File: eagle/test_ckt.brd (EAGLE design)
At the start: 152.4 x 152.4 mm, 38 parts, among them IC1 LT1352PA, T1 2N3904, T2 2N3904

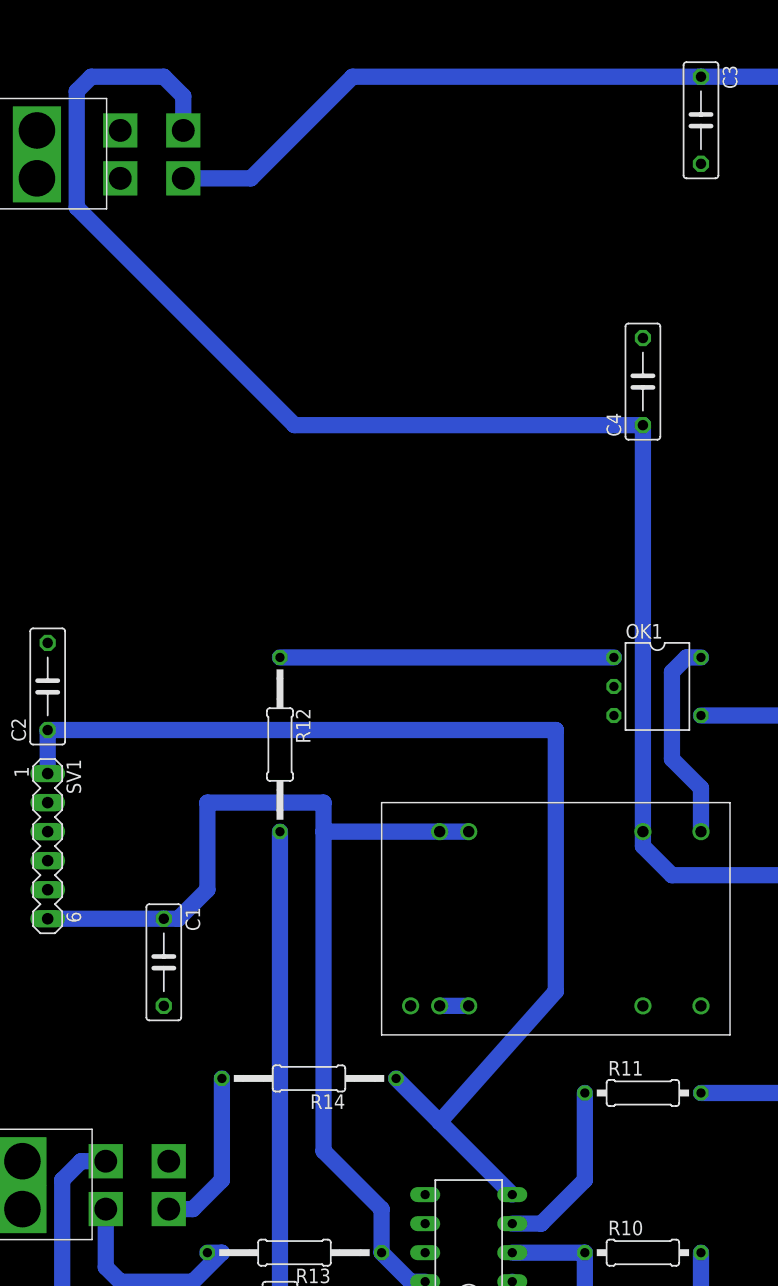
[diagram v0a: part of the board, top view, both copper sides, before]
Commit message: Fix pin assignment minifit Jr
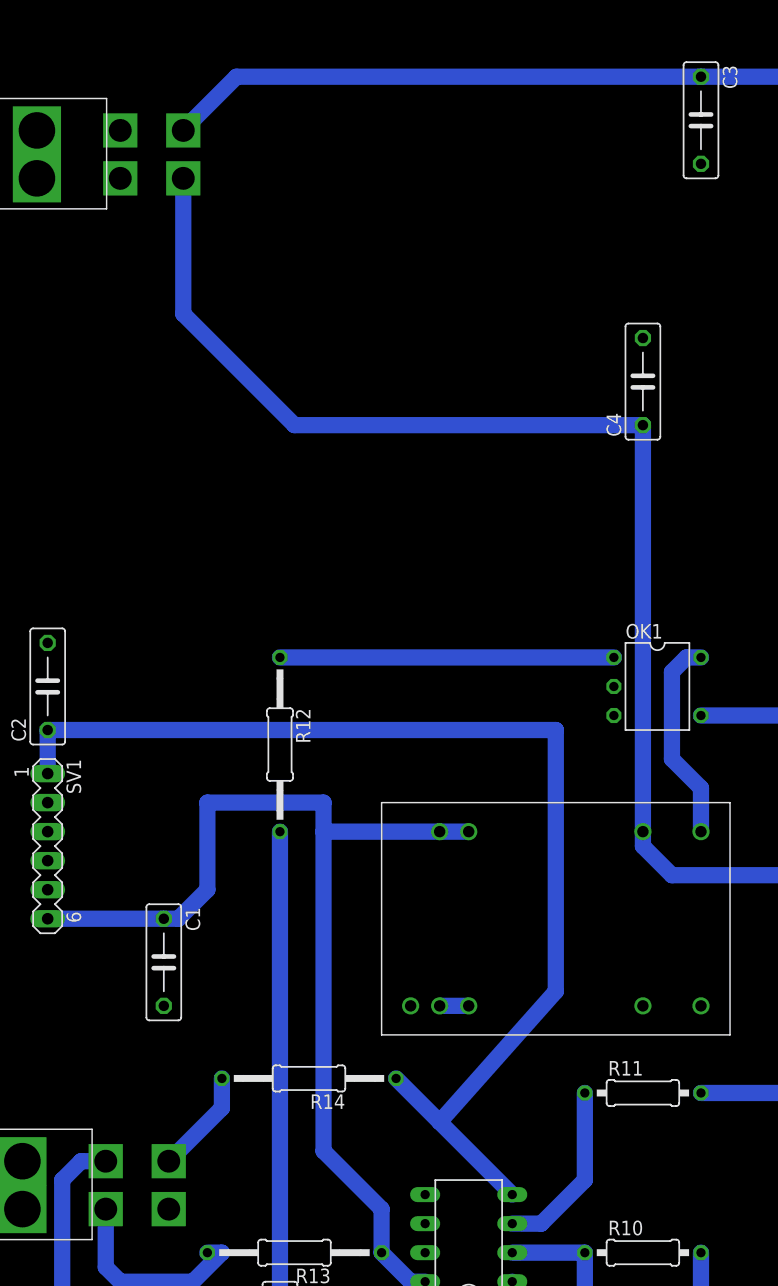
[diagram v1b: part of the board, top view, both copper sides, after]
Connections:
- net N$15: now also U$1.P$4; no longer U$1.P$3
- net V+: now also U$2.P$4; no longer U$2.P$3
- net V-: now also U$2.P$3; no longer U$2.P$4
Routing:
- net V-: track 164.7 -> 139.7 mm
- net N$15: track 14.6 -> 9.16 mm
- net V+: track 101.0 -> 99.5 mm
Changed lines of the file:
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@@
 <wire x1="104.14" y1="125.73" x2="85.09" y2="125.73" width="1.4224" layer="16"/>
 <wire x1="85.09" y1="125.73" x2="66.04" y2="125.73" width="1.4224" layer="16"/>
-<wire x1="66.04" y1="125.73" x2="35.56" y2="125.73" width="1.4224" layer="16"/>
-<wire x1="35.56" y1="125.73" x2="26.67" y2="116.84" width="1.4224" layer="16"/>
-<wire x1="26.67" y1="116.84" x2="20.32" y2="116.84" width="1.4224" layer="16"/>
-<contactref element="U$2" pad="P$3"/>
-<wire x1="20.7518" y1="116.84" x2="20.32" y2="116.84" width="0" layer="19" extent="16-16"/>
+<wire x1="66.04" y1="125.73" x2="25.4" y2="125.73" width="1.4224" layer="16"/>
+<contactref element="U$2" pad="P$4"/>
+<wire x1="25.4" y1="125.73" x2="20.32" y2="120.65" width="1.4224" layer="16"/>
+<wire x1="20.32" y1="120.65" x2="20.7518" y2="121.031" width="0" layer="19" extent="16-16"/>
 </signal>
 <signal name="V-">
@@
 <wire x1="76.2" y1="55.88" x2="76.2" y2="59.69" width="1.4224" layer="16"/>
 <wire x1="60.96" y1="59.69" x2="60.96" y2="95.25" width="1.4224" layer="16"/>
-<wire x1="11.43" y1="114.3" x2="30.48" y2="95.25" width="1.4224" layer="16"/>
 <wire x1="30.48" y1="95.25" x2="60.96" y2="95.25" width="1.4224" layer="16"/>
-<contactref element="U$2" pad="P$4"/>
-<wire x1="20.7518" y1="121.031" x2="20.7518" y2="124.0282" width="1.4224" layer="16"/>
-<wire x1="20.7518" y1="124.0282" x2="19.05" y2="125.73" width="1.4224" layer="16"/>
-<wire x1="19.05" y1="125.73" x2="12.7" y2="125.73" width="1.4224" layer="16"/>
-<wire x1="12.7" y1="125.73" x2="11.43" y2="124.46" width="1.4224" layer="16"/>
-<wire x1="11.43" y1="124.46" x2="11.43" y2="114.3" width="1.4224" layer="16"/>
+<contactref element="U$2" pad="P$3"/>
+<wire x1="20.7518" y1="116.84" x2="20.7518" y2="104.9782" width="1.4224" layer="16"/>
+<wire x1="20.7518" y1="104.9782" x2="30.48" y2="95.25" width="1.4224" layer="16"/>
 </signal>
 <signal name="N$6">
@@
 <signal name="N$15">
 <contactref element="R14" pad="2"/>
-<contactref element="U$1" pad="P$3"/>
-<wire x1="19.4818" y1="26.67" x2="21.59" y2="26.67" width="1.4224" layer="16"/>
-<wire x1="21.59" y1="26.67" x2="24.13" y2="29.21" width="1.4224" layer="16"/>
-<wire x1="24.13" y1="29.21" x2="24.13" y2="38.1" width="1.4224" layer="16"/>
+<contactref element="U$1" pad="P$4"/>
+<wire x1="24.13" y1="38.1" x2="24.13" y2="35.5092" width="1.4224" layer="16"/>
+<wire x1="24.13" y1="35.5092" x2="19.4818" y2="30.861" width="1.4224" layer="16"/>
 </signal>
 </signals>
